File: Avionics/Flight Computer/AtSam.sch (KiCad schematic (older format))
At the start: 39 parts, among them U12 ATSAME70Q21A-AN, Y1 9HT11-32.768KDZB-T, Y2 7V-16.000MAHJ-T

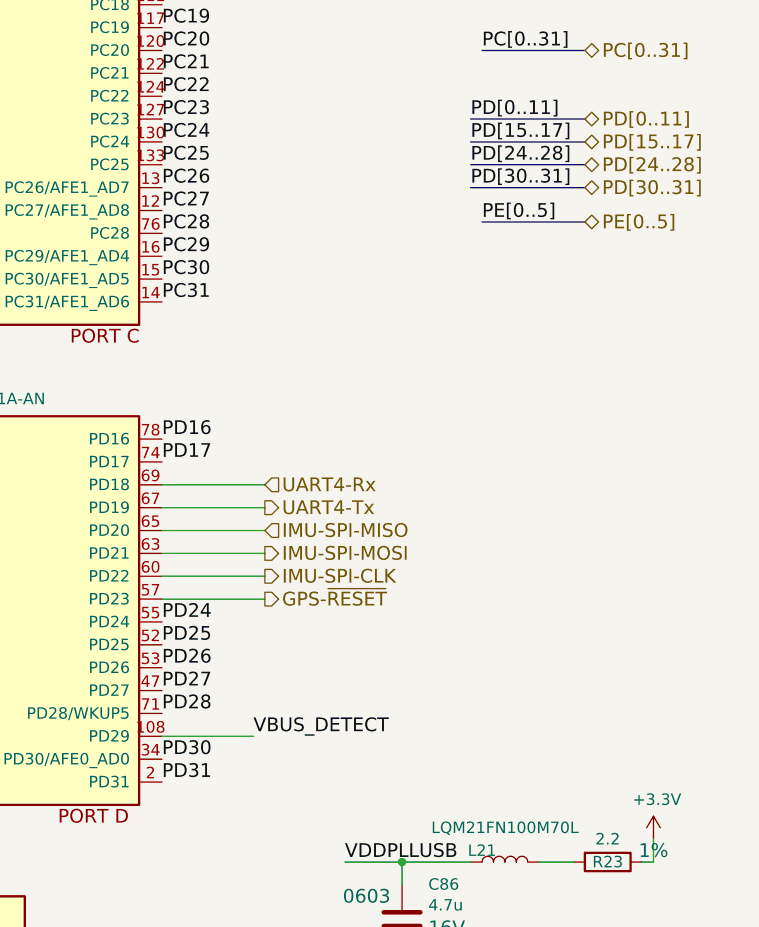
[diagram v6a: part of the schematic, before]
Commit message: Some more pin swapping and routing of signals. Placed reset pullup resistors.
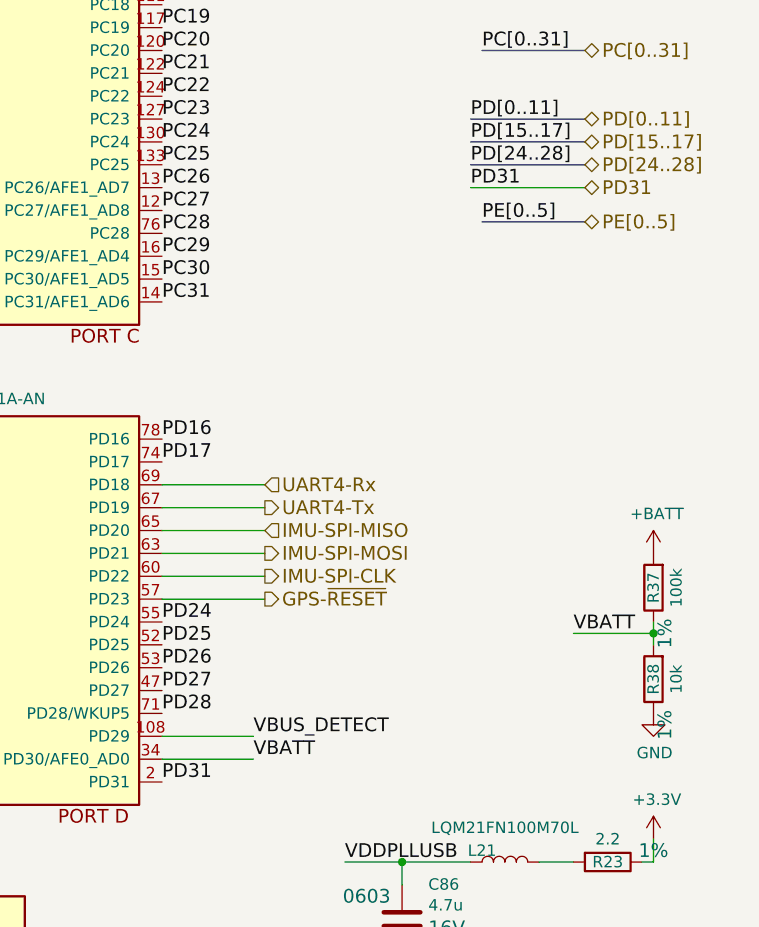
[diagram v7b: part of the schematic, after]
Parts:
- added R37: 100k, Resistors_SMD:R_0402, symbol R
- added R38: 10k, Resistors_SMD:R_0402, symbol R
- TP1, TP2, TP3: footprint Measurement_Points:Measurement_Point_Round-SMD-Pad_Small -> Measurement_Points:Measurement_Point_Round-SMD-Pad_Very_Small
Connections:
- net GND: now also R38.1
- net PD30 renamed VBATT
- net VBATT: now also R37.1, R38.2
- new net +BATT: R37.2
